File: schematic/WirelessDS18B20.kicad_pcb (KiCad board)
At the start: 2 copper layers, 25.4 x 30.5 mm, 14 parts, among them P1 Power Connector, P2 1-Wire Bus, P3 SERIAL_TX, Q1 BS170, SW1 SW_Push, SW2 SW_Push, U1 AMS1117-3.3, U2 ESP-01

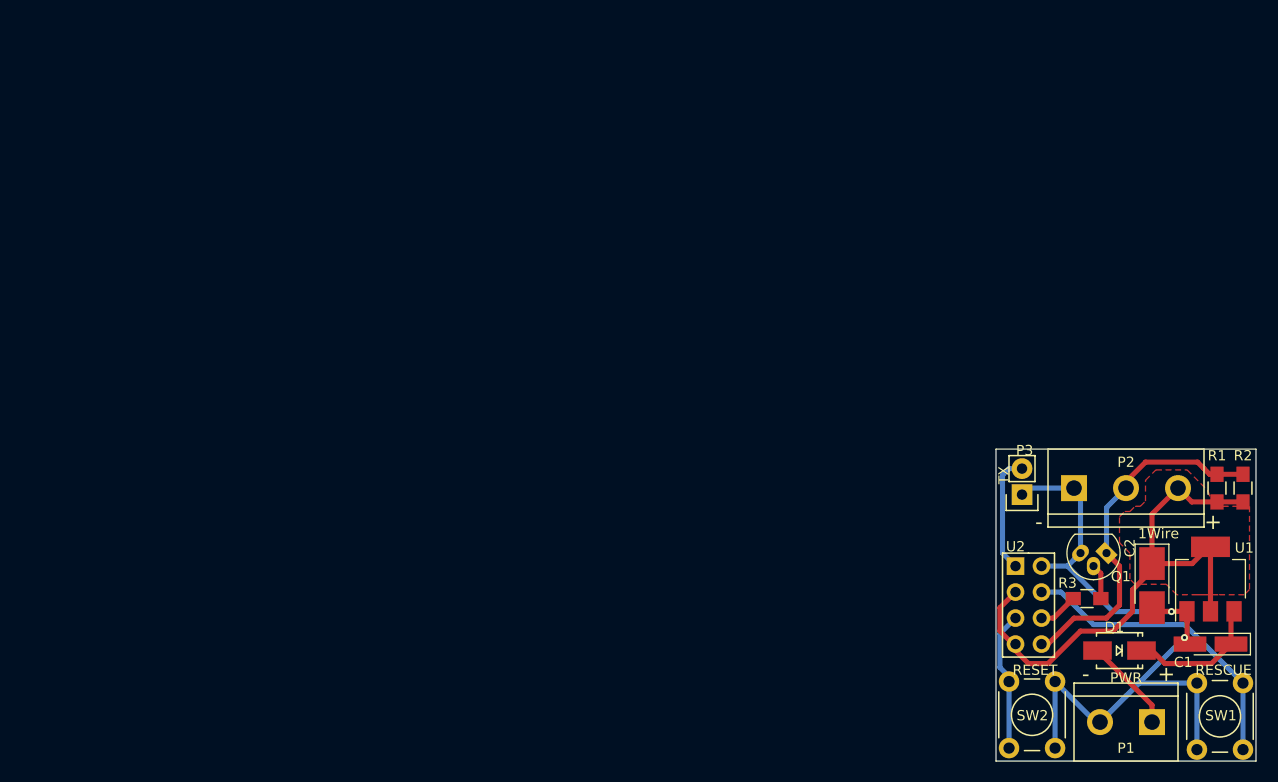
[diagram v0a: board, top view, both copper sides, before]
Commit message: Switch schematic to D1 Mini
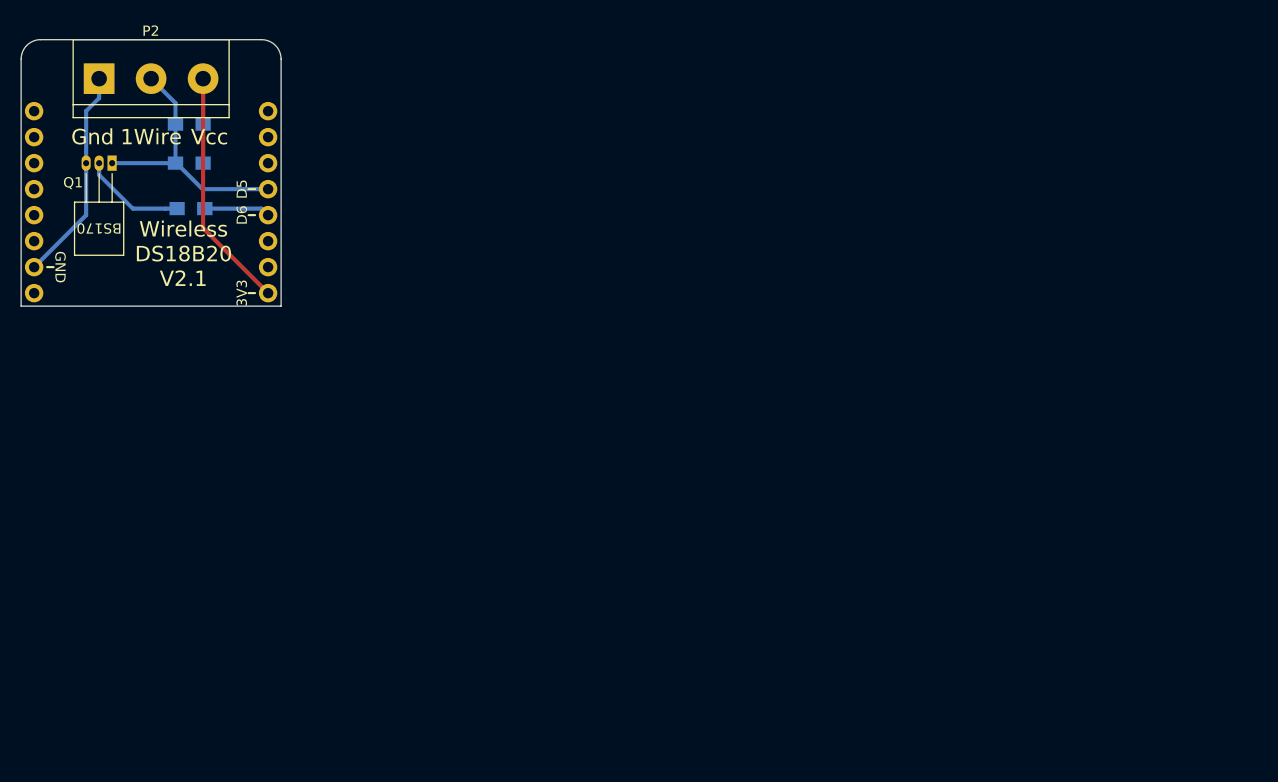
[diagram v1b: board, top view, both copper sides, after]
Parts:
- removed C1: 10uF, Capacitors_Tantalum_SMD:CP_Tantalum_Case-A_EIA-3216-18_Hand
- removed C2: 100uF, Capacitors_Tantalum_SMD:CP_Tantalum_Case-B_EIA-3528-21_Hand
- removed D1: SS34, Diodes_SMD_Custom:SMA_Handsoldering_Custom
- removed P1: Power Connector, Connect:bornier2
- removed P3: SERIAL_TX, Pin_Headers:Pin_Header_Straight_1x02
- removed SW1, SW2: SW_Push, Buttons_Switches_ThroughHole:SW_PUSH_6mm
- removed U2: ESP-01, ESP8266:ESP-01
- P2: footprint Connect:bornier3 -> Terminal_Blocks:TerminalBlock_bornier-3_P5.08mm
- Q1: footprint TO_SOT_Packages_THT:TO-92_Molded_Narrow_Oval -> TO_SOT_Packages_THT:TO-92_Horizontal2_Inline_Narrow_Oval
- R1, R2, R3: moved to B.Cu
- U1: value AMS1117-3.3 -> WeMos_mini; footprint TO_SOT_Packages_SMD:SOT-223 -> wemos_d1_mini:wemos-d1-mini-DIL-only; moved to B.Cu
- moved U1 109.9 mm to (36.2, 40.6)
- moved R2 108.9 mm to (39.9, 33.0), turned to 180 degrees
- moved P2 108.0 mm to (31.1, 28.6)
- moved R1 105.3 mm to (39.9, 36.8), turned to 180 degrees
- moved Q1 104.4 mm to (32.4, 36.8)
- moved R3 95.5 mm to (40.1, 41.3), turned to 180 degrees
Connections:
- U1 pad 1: GND -> (no net)
- U1 pad 2: VCC -> GND
- U1 pad 3: Net-(C1-Pad1) -> (no net)
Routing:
- net GND: track 81.0 -> 21.0 mm, vias 2 -> 0
- net Net-(SW1-Pad1): track 29.9 -> 0.00 mm
- net VCC: track 54.6 -> 32.5 mm
- net Net-(SW2-Pad1): track 13.7 -> 0.00 mm
- net Net-(C1-Pad1): track 13.6 -> 0.00 mm
- net Net-(P3-Pad2): track 11.6 -> 0.00 mm
- net Net-(P2-Pad2): track 35.3 -> 24.9 mm
- net Net-(D1-Pad2): track 9.19 -> 0.00 mm
- net Net-(Q1-Pad2): track 3.47 -> 10.1 mm
- net Net-(R3-Pad1): track 3.88 -> 6.45 mm
- removed copper zone on F.Cu, net VCC
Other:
- board size 25.4 x 30.5 mm -> 25.4 x 26 mm
- net class Default: trace_width 0.5 -> 0.4; via_dia 0.6858 -> 0.7; via_drill 0.3302 -> 0.4
- rule trace_min: 0.1524 -> 0.2
- rule via_min_drill: 0.3302 -> 0.3
- rule via_min_size: 0.6858 -> 0.4
- board text added: "2.2K"
- board text added: "3V3"
- board text added: "BS170"
- board text added: "D5"
- board text added: "D6"
- board text added: "GND"
- board text added: "Gnd"
- board text added: "Vcc"
- board text added: "Wireless DS18B20 V2.1"
- board text removed: "+"
- board text removed: "-"
- board text removed: "PWR"
- board text removed: "RESCUE"
- board text removed: "RESET"
- board text removed: "TX"
- board text removed: "V1.2"
- board text removed: "Wireless DS18B20"

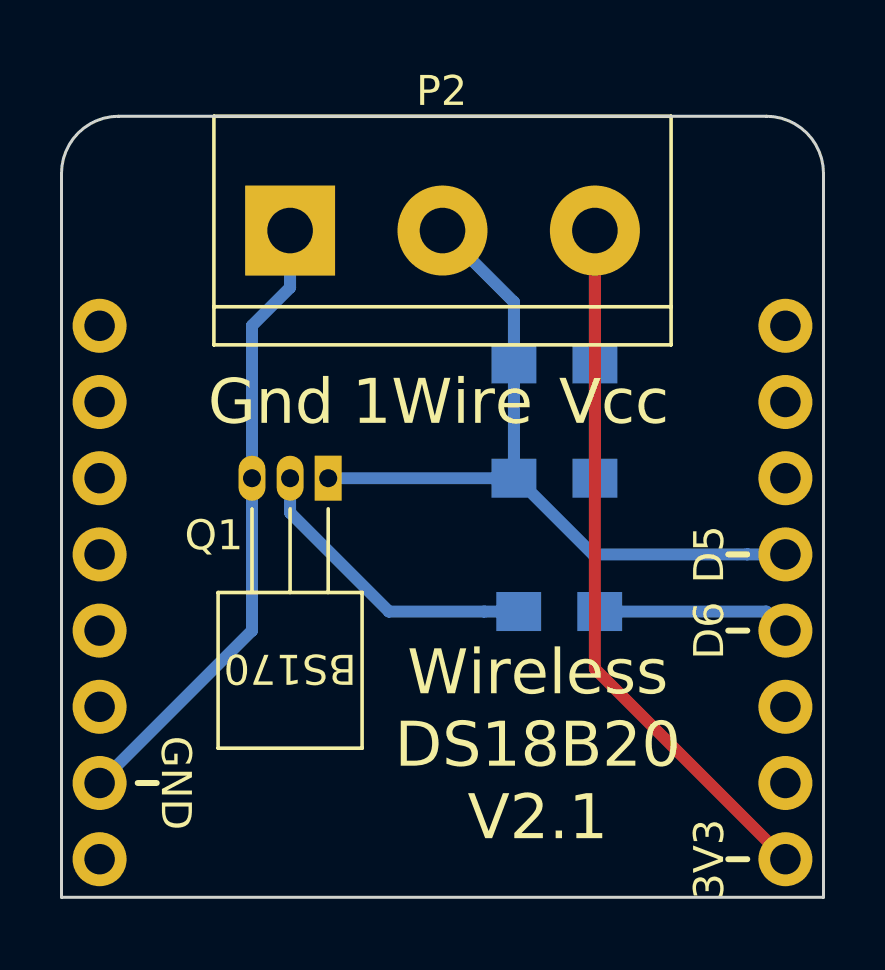
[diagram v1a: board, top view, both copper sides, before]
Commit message: Update schematic - add Optional power for large network
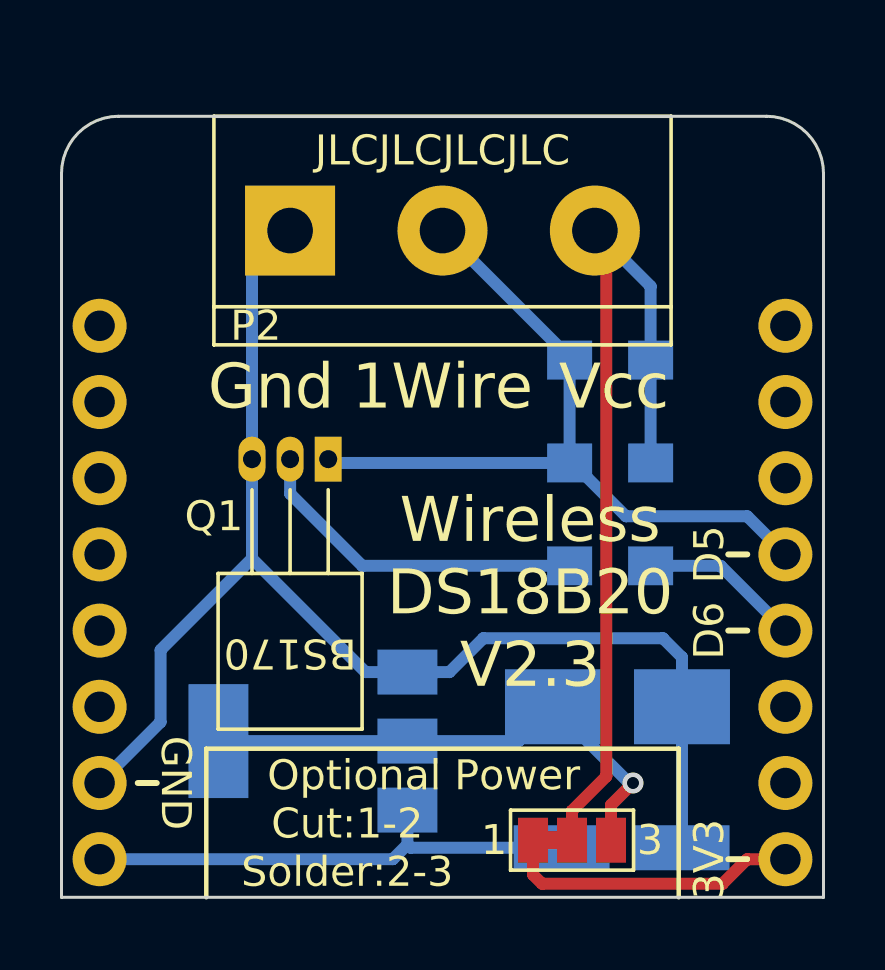
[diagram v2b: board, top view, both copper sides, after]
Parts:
- added C1: 10u, Capacitors_Tantalum_SMD:CP_Tantalum_Case-A_EIA-3216-18_Hand, B.Cu at (42.2, 49.1)
- added C2: 100u, Capacitors_Tantalum_SMD:CP_Tantalum_Case-B_EIA-3528-21_Hand, B.Cu at (42.0, 44.5)
- added JP1: SldrJmp_3_Bridged12, Jumper:SolderJumper-3_P1.3mm_Bridged12_Pad1.0x1.5mm_NumberLabels, F.Cu at (40.5, 48.9)
- added U2: AMS1117-3.3, TO_SOT_Packages_SMD:SOT-223-3_TabPin2, B.Cu at (31.9, 45.6)
- moved R1 4.35 mm to (41.8, 32.9)
- moved R2 3.79 mm to (41.8, 36.3)
- moved R3 2.28 mm to (41.8, 39.8)
- moved Q1 0.63 mm to (32.4, 36.2)
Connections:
- U1 pad 1: (no net) -> /5V
- U1 pad 16: VCC -> /3V3
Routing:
- net GND: track 21.0 -> 44.0 mm
- net Net-(C2-Pad1): track 0.00 -> 17.6 mm, vias 0 -> 1
- net /5V: track 0.00 -> 16.8 mm
- net /3V3: track 0.00 -> 10.0 mm
- net VCC: track 32.5 -> 29.5 mm
- net Net-(Q1-Pad2): track 10.1 -> 11.5 mm
- net Net-(P2-Pad2): track 24.9 -> 26.1 mm
- net Net-(R3-Pad1): track 6.45 -> 5.39 mm
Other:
- board text added: "Cut:1-2 Solder:2-3"
- board text added: "JLCJLCJLCJLC"
- board text added: "Optional Power"
- board text added: "Wireless DS18B20 V2.3"
- board text removed: "2.2K"
- board text removed: "BS170"
- board text removed: "Wireless DS18B20 V2.1"

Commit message: Update schematic
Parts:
- C1: footprint Capacitors_Tantalum_SMD:CP_Tantalum_Case-A_EIA-3216-18_Hand -> Capacitor_Tantalum_SMD:CP_EIA-3216-18_Kemet-A_Pad1.58x1.35mm_HandSolder
- C2: footprint Capacitors_Tantalum_SMD:CP_Tantalum_Case-B_EIA-3528-21_Hand -> Capacitor_Tantalum_SMD:CP_EIA-3528-21_Kemet-B_Pad1.50x2.35mm_HandSolder
- P2: footprint Terminal_Blocks:TerminalBlock_bornier-3_P5.08mm -> TerminalBlock:TerminalBlock_bornier-3_P5.08mm
- Q1: footprint TO_SOT_Packages_THT:TO-92_Horizontal2_Inline_Narrow_Oval -> Package_TO_SOT_THT:TO-92_Inline_Horizontal2
- R1, R2, R3: footprint Resistors_SMD:R_0805_HandSoldering -> Resistor_SMD:R_0805_2012Metric_Pad1.15x1.40mm_HandSolder
- U2: footprint TO_SOT_Packages_SMD:SOT-223-3_TabPin2 -> Package_TO_SOT_SMD:SOT-223-3_TabPin2
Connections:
- net /3V3 renamed 3V3
- net /5V renamed 5V
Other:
- board text added: "DomoChip Wireless DS18B20 V2.3"
- board text removed: "Wireless DS18B20 V2.3"

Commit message: Update schematic to KiCAD8
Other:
- net class Default removed

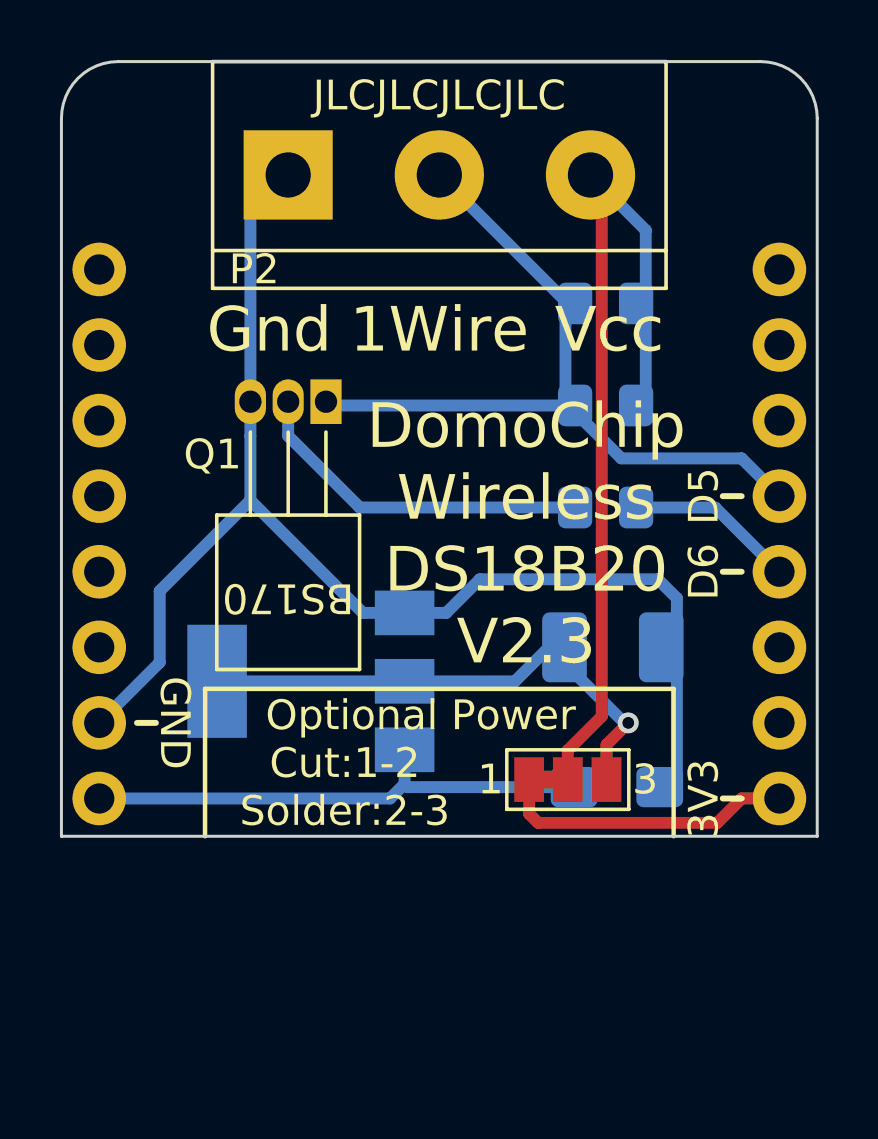
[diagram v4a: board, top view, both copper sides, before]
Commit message: V3.0 of the PCB (additional power is not optional)
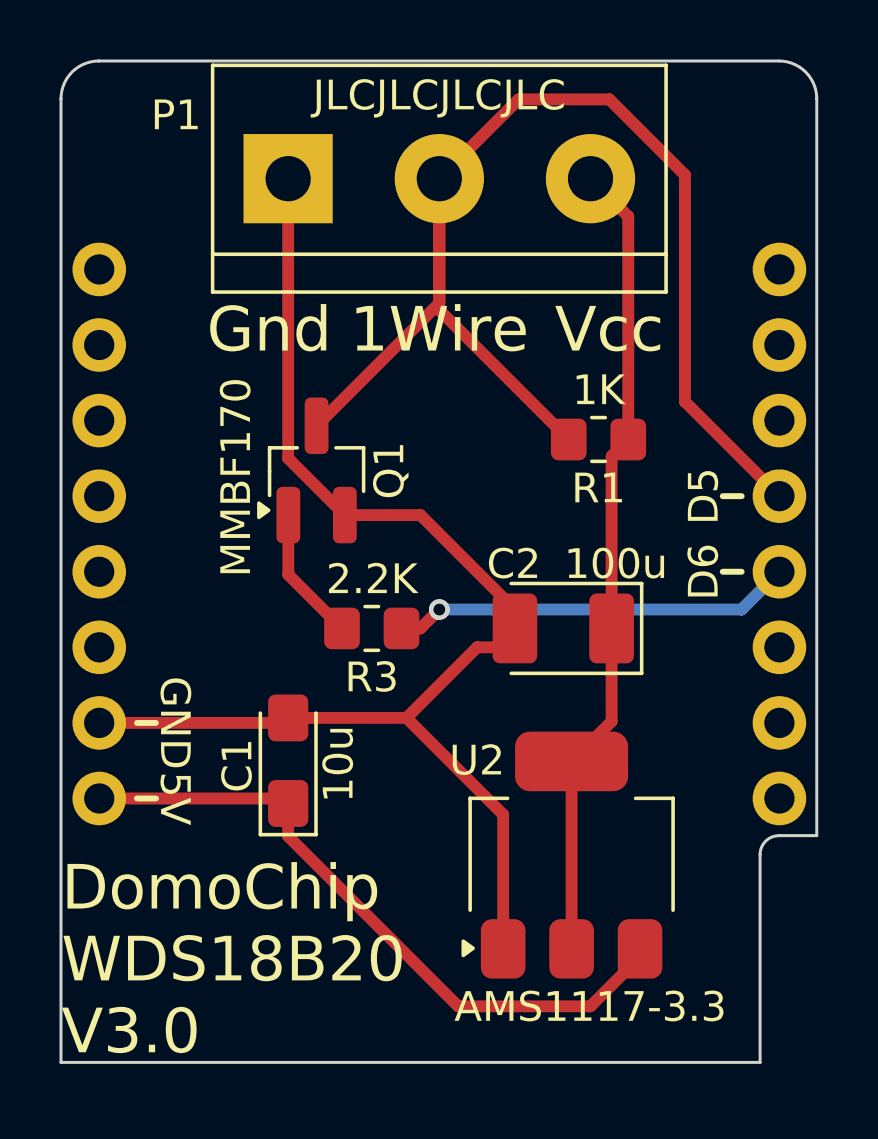
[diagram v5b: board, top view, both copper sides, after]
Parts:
- removed JP1: SldrJmp_3_Bridged12, Jumper:SolderJumper-3_P1.3mm_Bridged12_Pad1.0x1.5mm_NumberLabels
- removed R2: 2.2K, Resistor_SMD:R_0805_2012Metric_Pad1.15x1.40mm_HandSolder
- C1, C2, U2: moved to F.Cu
- Q1: value BS170 -> MMBF170; footprint Package_TO_SOT_THT:TO-92_Inline_Horizontal2 -> Package_TO_SOT_SMD:SOT-23_Handsoldering
- R1: value 2.2K -> 1K; footprint Resistor_SMD:R_0805_2012Metric_Pad1.15x1.40mm_HandSolder -> Resistor_SMD:R_0805_2012Metric_Pad1.20x1.40mm_HandSolder; moved to F.Cu
- R3: footprint Resistor_SMD:R_0805_2012Metric_Pad1.15x1.40mm_HandSolder -> Resistor_SMD:R_0805_2012Metric_Pad1.20x1.40mm_HandSolder; moved to F.Cu
- moved C1 11.1 mm to (31.1, 48.3), turned to 90 degrees
- moved U2 10.5 mm to (40.6, 51.4), turned to 90 degrees
- moved R3 8.85 mm to (33.9, 43.8)
- moved R1 4.58 mm to (41.5, 37.5)
- moved Q1 2.33 mm to (32.1, 38.5), turned to 90 degrees
- moved C2 1.78 mm to (40.4, 43.8), turned to 180 degrees
- moved P1 0.12 mm to (31.1, 28.7)
- renumbered P2 to P1
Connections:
- C2 pad 1: Net-(C2-Pad1) -> VCC
- P1 pad 2: Net-(P2-Pad2) -> Net-(P1-Pin_2)
- Q1 pad 1: Net-(P2-Pad2) -> Net-(Q1-G)
- Q1 pad 2: Net-(Q1-Pad2) -> GND
- Q1 pad 3: GND -> Net-(P1-Pin_2)
- R1 pad 2: Net-(P2-Pad2) -> Net-(P1-Pin_2)
- R3 pad 2: Net-(Q1-Pad2) -> Net-(Q1-G)
- U1 pad 10: (no net) -> unconnected-(U1-A0-Pad10)
- U1 pad 11: (no net) -> unconnected-(U1-D0-Pad11)
- U1 pad 12: Net-(P2-Pad2) -> Net-(P1-Pin_2)
- U1 pad 14: (no net) -> unconnected-(U1-D7-Pad14)
- U1 pad 15: (no net) -> unconnected-(U1-D8-Pad15)
- U1 pad 16: 3V3 -> unconnected-(U1-3.3V-Pad16)
- U1 pad 3: (no net) -> unconnected-(U1-D4-Pad3)
- U1 pad 4: (no net) -> unconnected-(U1-D3-Pad4)
- U1 pad 5: (no net) -> unconnected-(U1-D2-Pad5)
- U1 pad 6: (no net) -> unconnected-(U1-D1-Pad6)
- U1 pad 7: (no net) -> unconnected-(U1-Rx-Pad7)
- U1 pad 8: (no net) -> unconnected-(U1-Tx-Pad8)
- U1 pad 9: (no net) -> unconnected-(U1-Rst-Pad9)
- U2 pad 2: Net-(C2-Pad1) -> VCC
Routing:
- net Net-(P1-Pin_2): track 0.00 -> 43.1 mm
- net Net-(P2-Pad2): track 26.1 -> 0.00 mm
- net Net-(C2-Pad1): track 17.6 -> 0.00 mm, vias 1 -> 0
- net Net-(Q1-Pad2): track 11.5 -> 0.00 mm
- net 3V3: track 10.0 -> 0.00 mm
- net Net-(U1-D6): track 5.39 -> 13.5 mm, vias 0 -> 1
- net 5V: track 16.8 -> 22.2 mm
- net Net-(Q1-G): track 0.00 -> 4.56 mm
- net VCC: track 29.5 -> 27.2 mm
- net GND: track 44.0 -> 43.3 mm
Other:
- board size 25.4 x 26 mm -> 25.4 x 33.7 mm
- board text added: "5V"
- board text added: "DomoChip WDS18B20 V3.0"
- board text removed: "3V3"
- board text removed: "Cut:1-2 Solder:2-3"
- board text removed: "DomoChip Wireless DS18B20 V2.3"
- board text removed: "Optional Power"
